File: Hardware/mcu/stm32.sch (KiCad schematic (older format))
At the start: 35 parts, among them P1101 EXP1, P1102 EXP2, P1104 EXP4, P1105 EXPPWR, Q1101 NPN, SW1101 Reset, U1101 STM32F103ZC, U903 XO53, X1101 32KHz

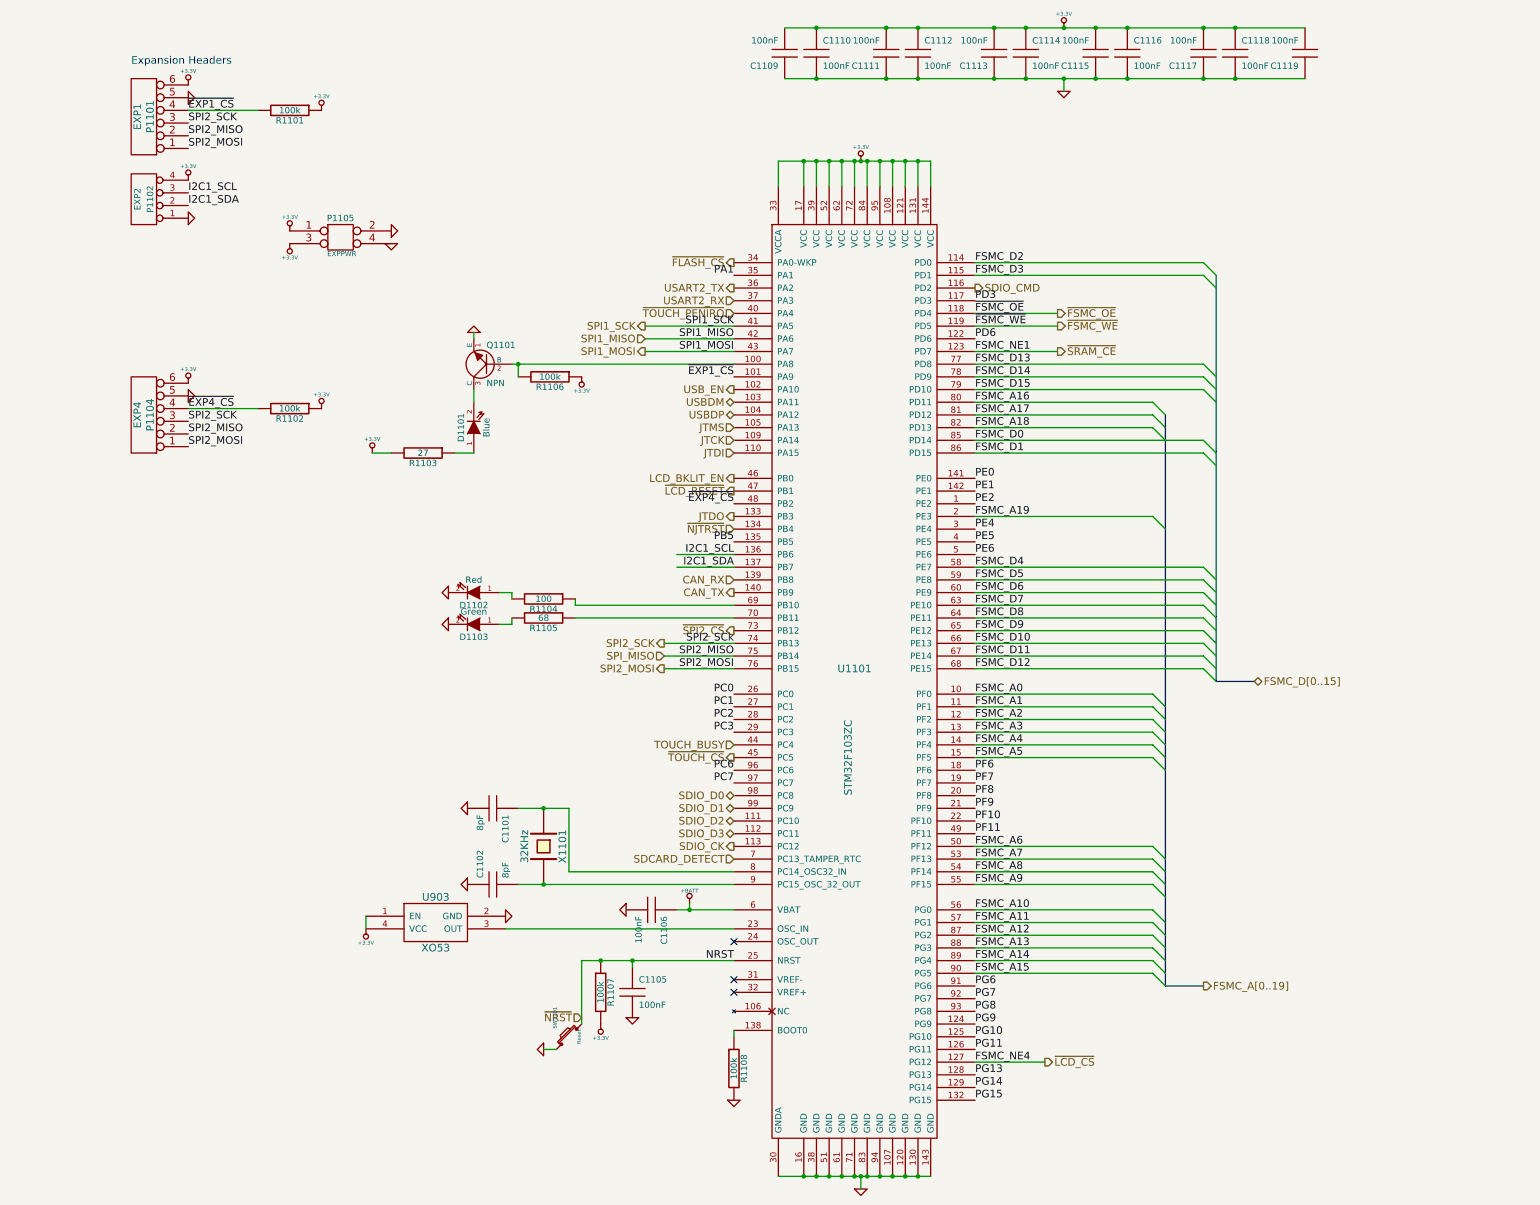
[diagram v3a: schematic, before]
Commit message: changes to mcu, new format and using a display adapter board
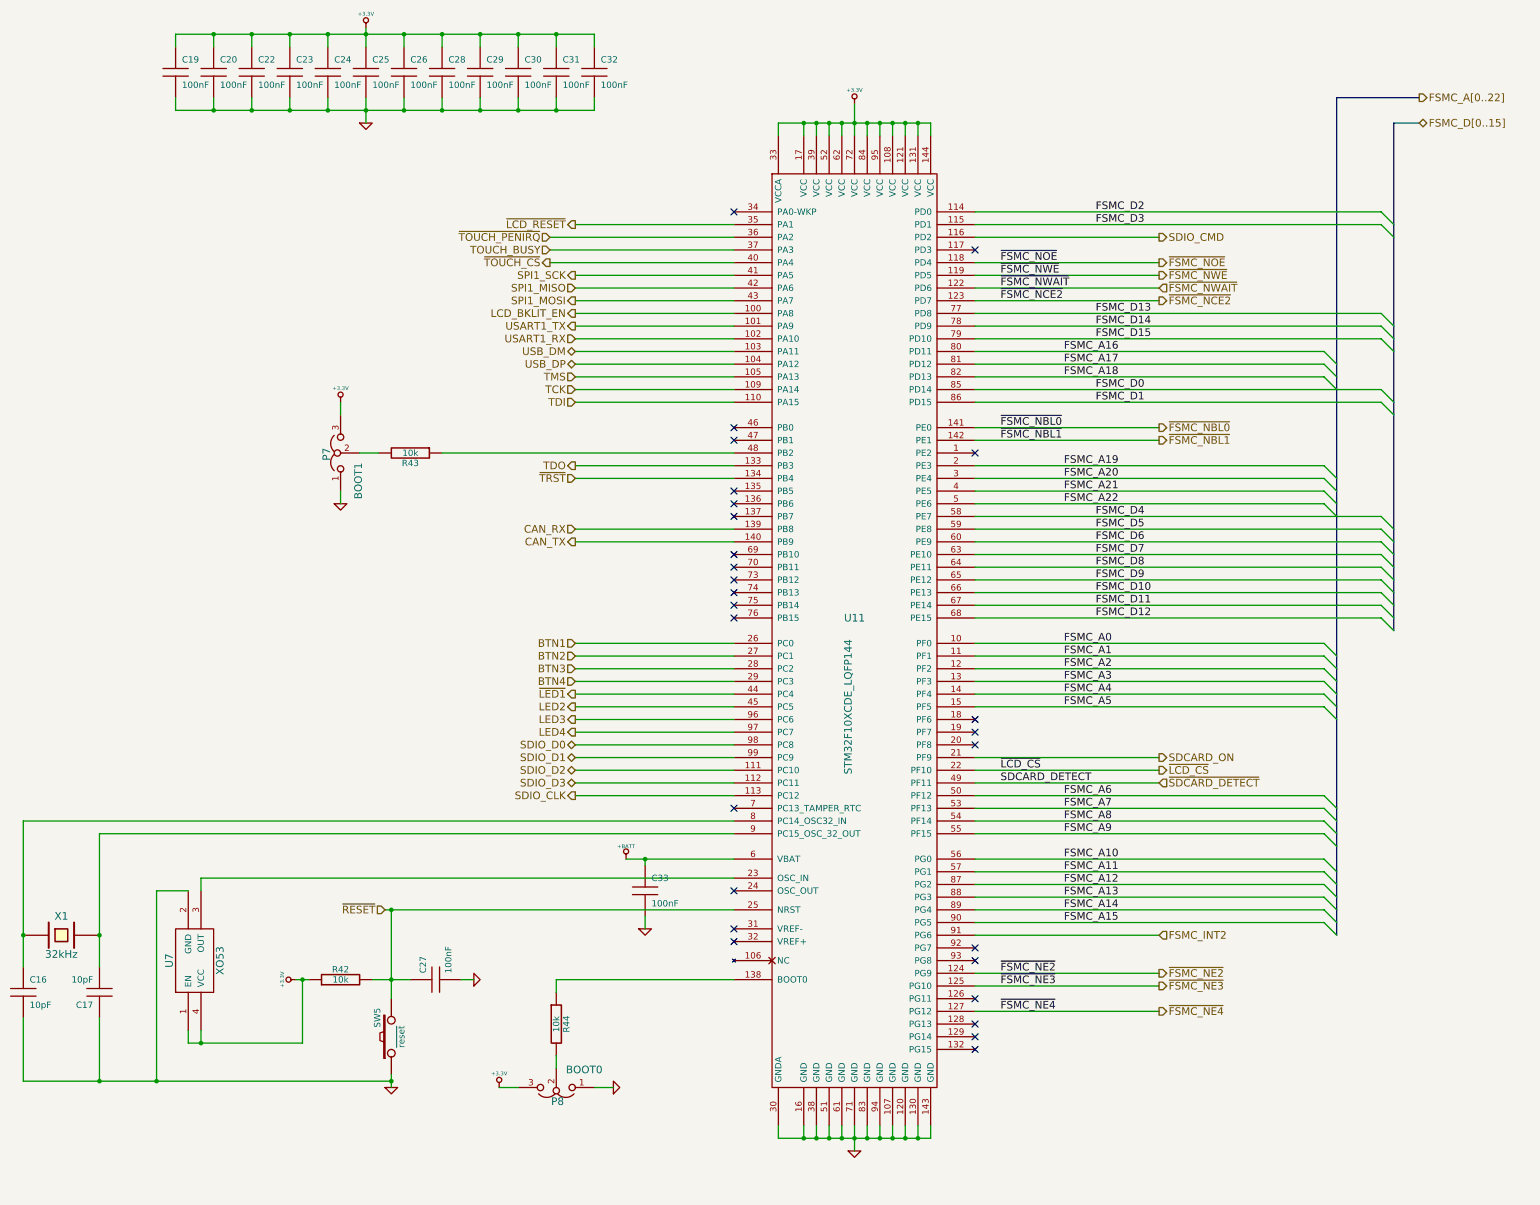
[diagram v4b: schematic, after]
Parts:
- removed C1101, C1102: 8pF, symbol C
- removed C1105, C1106, C1109, C1110, C1111, C1112, C1113, C1114, C1115, C1116, C1117, C1118, C1119: 100nF, symbol C
- removed D1101: Blue, symbol LED
- removed D1102: Red, symbol LED
- removed D1103: Green, symbol LED
- removed P1101: EXP1, symbol CONN_6
- removed P1102: EXP2, symbol CONN_4
- removed P1104: EXP4, symbol CONN_6
- removed P1105: EXPPWR, symbol CONN_2X2
- removed Q1101: NPN, symbol NPN
- removed R1101, R1102, R1106, R1107, R1108: 100k, symbol R
- removed R1103: 27, symbol R
- removed R1104: 100, symbol R
- removed R1105: 68, symbol R
- removed SW1101: Reset, symbol SW_PUSH_SMALL
- removed U1101: STM32F103ZC, symbol STM32F10XCDE_LQFP144
- removed U903: XO53, symbol XO53
- removed X1101: 32KHz, symbol CRYSTAL
- added C16, C17: 10pF, symbol C
- added C19, C20, C22, C23, C24, C25, C26, C27, C28, C29, C30, C31, C32, C33: 100nF, symbol C
- added P7: BOOT1, symbol JUMPER3
- added P8: BOOT0, symbol JUMPER3
- added R42, R43, R44: 10k, symbol R
- added SW5: ~reset, symbol SW_PUSH
- added U11: STM32F10XCDE_LQFP144, symbol STM32F10XCDE_LQFP144
- added U7: XO53, symbol XO53
- added X1: 32kHz, symbol CRYSTAL
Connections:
- net +3.3V: now also C19.1, C20.1, C22.1, C23.1, C24.1, C25.1, C26.1, C28.1, C29.1, C30.1, C31.1, C32.1, P7.3, P8.3, R42.1, U11.108 (VCC), U11.121 (VCC), U11.131 (VCC), U11.144 (VCC), U11.17 (VCC), U11.33 (VCCA), U11.39 (VCC), U11.52 (VCC), U11.62 (VCC), U11.72 (VCC), U11.84 (VCC), U11.95 (VCC), U7.1 (EN), U7.4 (VCC)
- net +BATT: now also C33.1, U11.6 (VBAT)
- net CAN_RX: now also U11.139 (PB8)
- net CAN_TX: now also U11.140 (PB9)
- net FSMC_A0: now also U11.10 (PF0)
- net FSMC_A1: now also U11.11 (PF1)
- net FSMC_A10: now also U11.56 (PG0)
- net FSMC_A11: now also U11.57 (PG1)
- net FSMC_A12: now also U11.87 (PG2)
- net FSMC_A13: now also U11.88 (PG3)
- net FSMC_A14: now also U11.89 (PG4)
- net FSMC_A15: now also U11.90 (PG5)
- net FSMC_A16: now also U11.80 (PD11)
- net FSMC_A17: now also U11.81 (PD12)
- net FSMC_A18: now also U11.82 (PD13)
- net FSMC_A19: now also U11.2 (PE3)
- net FSMC_A2: now also U11.12 (PF2)
- net FSMC_A3: now also U11.13 (PF3)
- net FSMC_A4: now also U11.14 (PF4)
- net FSMC_A5: now also U11.15 (PF5)
- net FSMC_A6: now also U11.50 (PF12)
- net FSMC_A7: now also U11.53 (PF13)
- net FSMC_A8: now also U11.54 (PF14)
- net FSMC_A9: now also U11.55 (PF15)
- net FSMC_D0: now also U11.85 (PD14)
- net FSMC_D1: now also U11.86 (PD15)
- net FSMC_D10: now also U11.66 (PE13)
- net FSMC_D11: now also U11.67 (PE14)
- net FSMC_D12: now also U11.68 (PE15)
- net FSMC_D13: now also U11.77 (PD8)
- net FSMC_D14: now also U11.78 (PD9)
- net FSMC_D15: now also U11.79 (PD10)
- net FSMC_D2: now also U11.114 (PD0)
- net FSMC_D3: now also U11.115 (PD1)
- net FSMC_D4: now also U11.58 (PE7)
- net FSMC_D5: now also U11.59 (PE8)
- net FSMC_D6: now also U11.60 (PE9)
- net FSMC_D7: now also U11.63 (PE10)
- net FSMC_D8: now also U11.64 (PE11)
- net FSMC_D9: now also U11.65 (PE12)
- net GND: now also C16.2, C17.1, C19.2, C20.2, C22.2, C23.2, C24.2, C25.2, C26.2, C27.2, C28.2, C29.2, C30.2, C31.2, C32.2, C33.2, P7.1, P8.1, SW5.1, U11.107 (GND), U11.120 (GND), U11.130 (GND), U11.143 (GND), U11.16 (GND), U11.30 (GNDA), U11.38 (GND), U11.51 (GND), U11.61 (GND), U11.71 (GND), U11.83 (GND), U11.94 (GND), U7.2 (GND)
- net LCD_BKLIT_EN: now also U11.100 (PA8)
- net SDIO_CMD: now also U11.116 (PD2)
- net SDIO_D0: now also U11.98 (PC8)
- net SDIO_D1: now also U11.99 (PC9)
- net SDIO_D2: now also U11.111 (PC10)
- net SDIO_D3: now also U11.112 (PC11)
- net SPI1_MISO: now also U11.42 (PA6)
- net SPI1_MOSI: now also U11.43 (PA7)
- net SPI1_SCK: now also U11.41 (PA5)
- net TOUCH_BUSY: now also U11.37 (PA3)
- net ~LCD_CS: now also U11.22 (PF10)
- net ~LCD_RESET: now also U11.35 (PA1)
- net ~TOUCH_CS: now also U11.40 (PA4)
- net ~TOUCH_PENIRQ: now also U11.36 (PA2)
- new net: R44.1, U11.138 (BOOT0)
- new net: U11.23 (OSC_IN), U7.3 (OUT)
- new net: R43.1, U11.48 (PB2)
- new net: C16.1, U11.8 (PC14_OSC32_IN), X1.1
- new net: C17.2, U11.9 (PC15_OSC_32_OUT), X1.2
- new net: P7.2, R43.2
- new net: P8.2, R44.2
- new net BTN1: U11.26 (PC0)
- new net BTN2: U11.27 (PC1)
- new net BTN3: U11.28 (PC2)
- new net BTN4: U11.29 (PC3)
- new net FSMC_A20: U11.3 (PE4)
- new net FSMC_A21: U11.4 (PE5)
- new net FSMC_A22: U11.5 (PE6)
- new net FSMC_INT2: U11.91 (PG6)
- new net LED2: U11.45 (PC5)
- new net LED3: U11.96 (PC6)
- new net LED4: U11.97 (PC7)
- new net SDCARD_ON: U11.21 (PF9)
- new net SDIO_CLK: U11.113 (PC12)
- new net TCK: U11.109 (PA14)
- new net TDI: U11.110 (PA15)
- new net TDO: U11.133 (PB3)
- new net TMS: U11.105 (PA13)
- new net USART1_RX: U11.102 (PA10)
- new net USART1_TX: U11.101 (PA9)
- new net USB_DM: U11.103 (PA11)
- new net USB_DP: U11.104 (PA12)
- new net ~FSMC_NBL0: U11.141 (PE0)
- new net ~FSMC_NBL1: U11.142 (PE1)
- new net ~FSMC_NCE2: U11.123 (PD7)
- new net ~FSMC_NE2: U11.124 (PG9)
- new net ~FSMC_NE3: U11.125 (PG10)
- new net ~FSMC_NE4: U11.127 (PG12)
- new net ~FSMC_NOE: U11.118 (PD4)
- new net ~FSMC_NWAIT: U11.122 (PD6)
- new net ~FSMC_NWE: U11.119 (PD5)
- new net ~LED1: U11.44 (PC4)
- new net ~RESET: C27.1, R42.2, SW5.2, U11.25 (NRST)
- new net ~SDCARD_DETECT: U11.49 (PF11)
- new net ~TRST: U11.134 (PB4)
- no-connect marks 3 -> 27
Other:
- note removed: "Expansion Headers"
